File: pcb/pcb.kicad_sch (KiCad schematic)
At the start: 0 parts

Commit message: added the components except the oled to the schematic
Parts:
- added SW1, SW2, SW3, SW4: SW_Push, symbol Switch:SW_Push
- added U1: XIAO-RP2040-DIP, Module:MOUDLE14P-XIAO-DIP-SMD, symbol Seeed_Studio_XIAO_Series:XIAO-RP2040-DIP
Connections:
- new net GND: SW1.2, SW2.2, SW3.2, SW4.2
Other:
- note added: "Switches/Buttons"

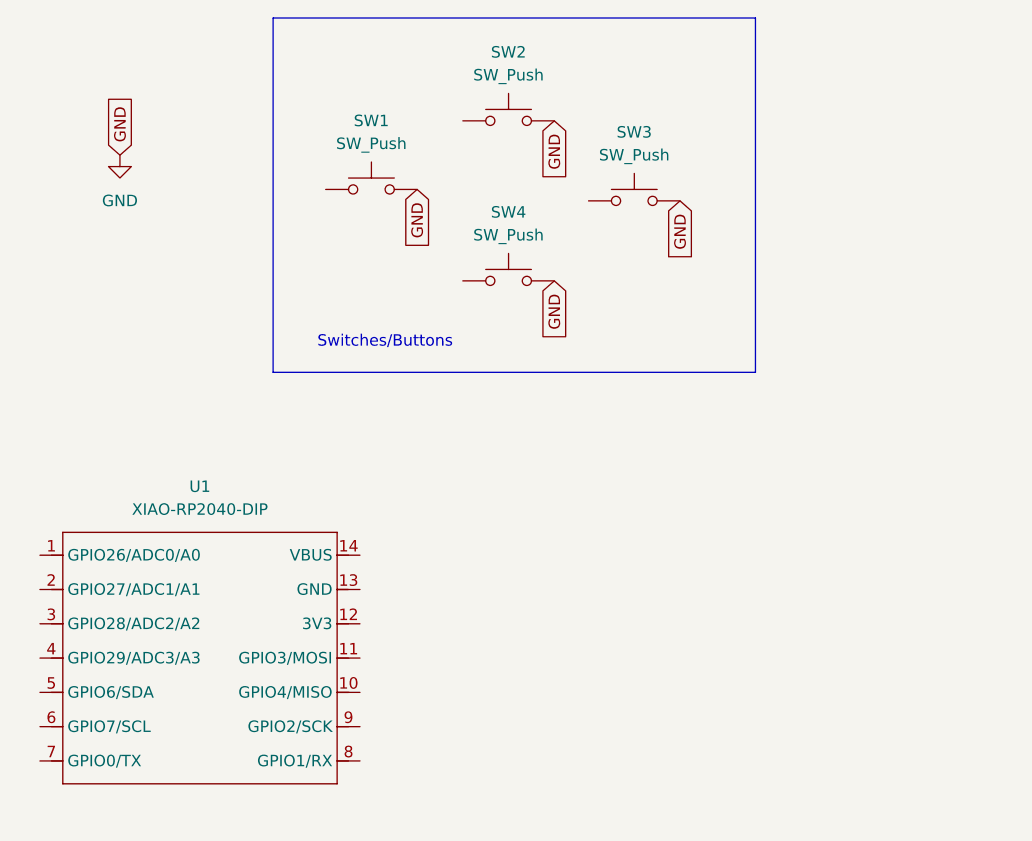
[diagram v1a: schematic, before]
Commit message: added the oled screen as well as needed connections
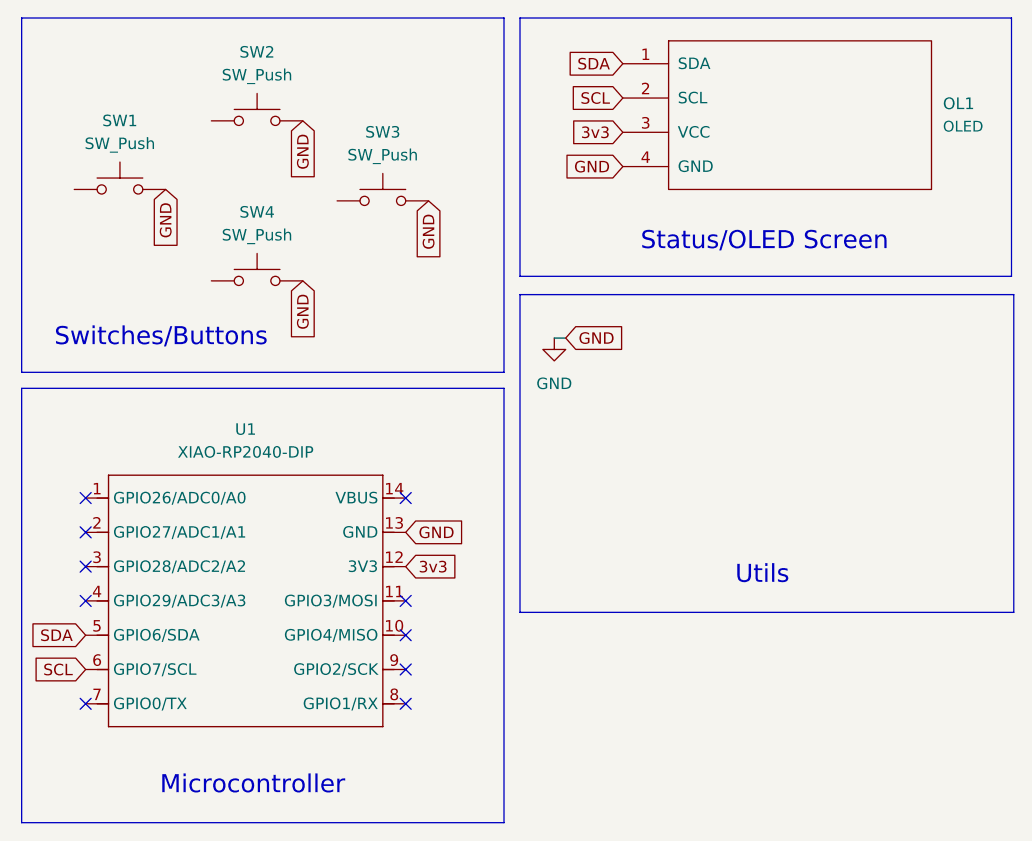
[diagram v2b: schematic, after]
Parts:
- added OL1: OLED, symbol kbd:OLED
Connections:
- net GND: now also U1.13 (GND), OL1.4 (GND)
- net 3v3: now reaches U1.12 (3V3)
- net 3v3: now also OL1.3 (VCC)
- net SDA: now reaches U1.5 (GPIO6/SDA)
- net SDA: now also OL1.1 (SDA)
- net SCL: now reaches U1.6 (GPIO7/SCL)
- net SCL: now also OL1.2 (SCL)
- no-connect marks 0 -> 10
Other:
- note added: "Microcontroller"
- note added: "Status/OLED Screen"
- note added: "Utils"
- moved on the sheet: SW1, SW2, SW3, SW4, U1
